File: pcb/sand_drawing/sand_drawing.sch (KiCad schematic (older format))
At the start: 13 parts, among them J0 12VDC, J1 Stepper1, J2 Stepper2, J3 Arm 1 Opto, J4 Arm 2 Opto, J5 ESP POWER, J6 Unused Pins, U1 WeMos_D1_mini, U2 LD1117_TO220

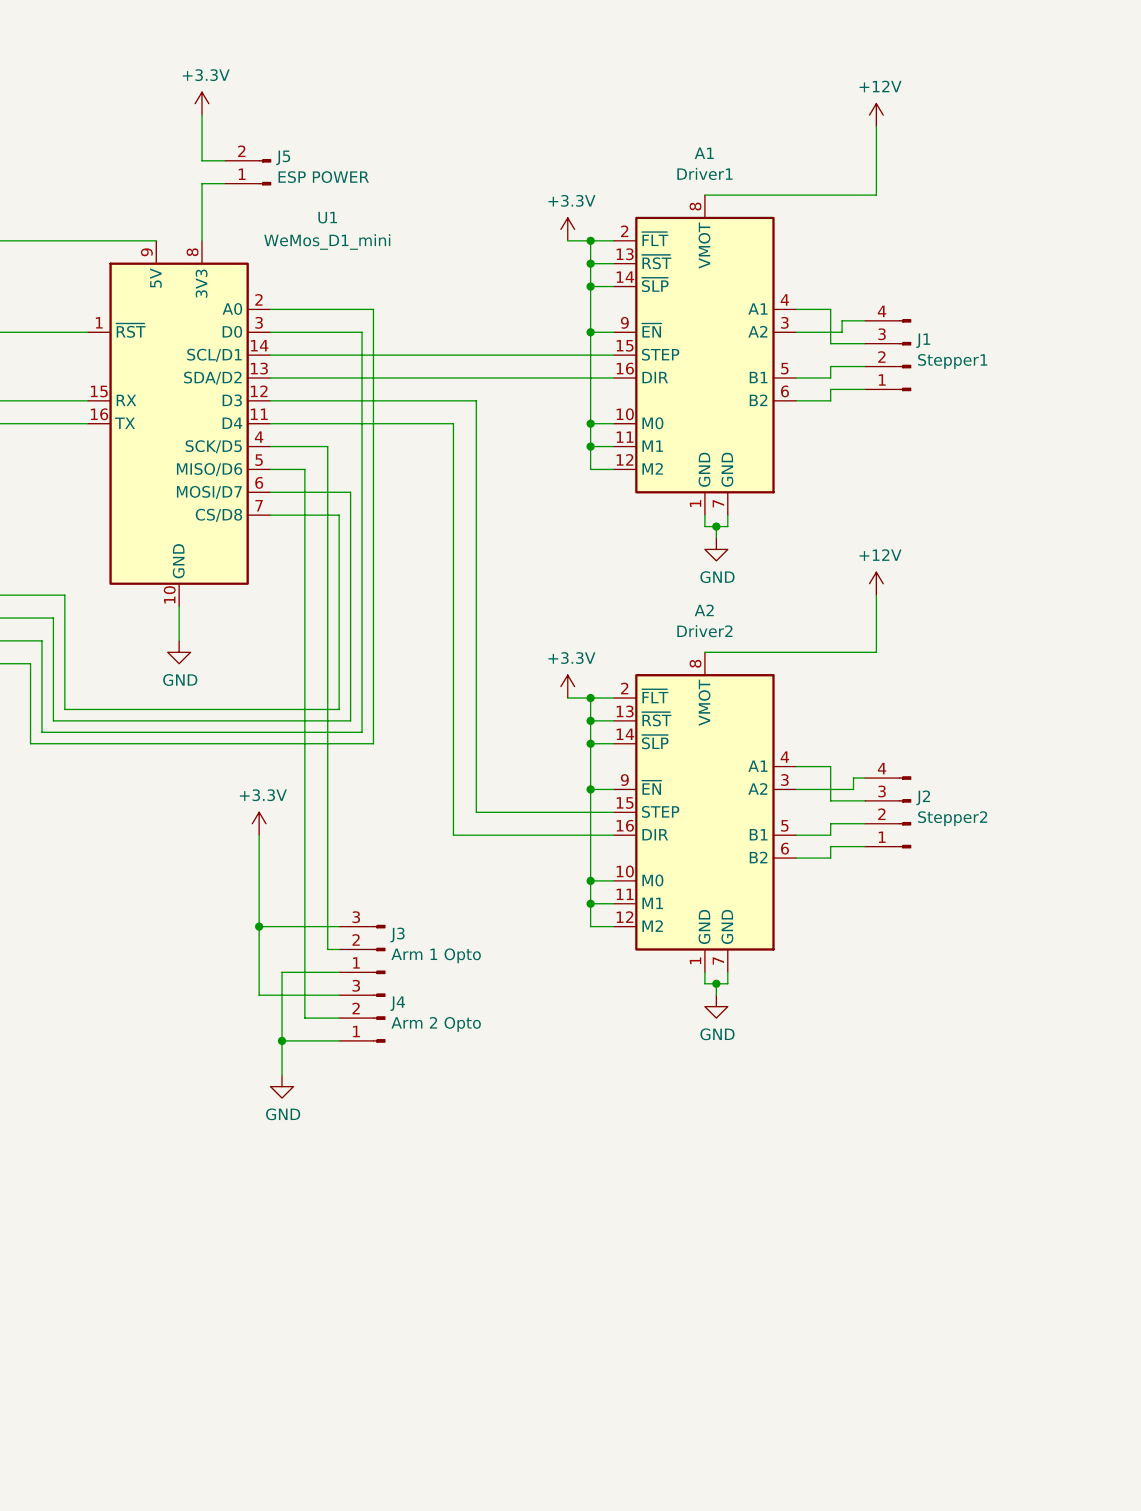
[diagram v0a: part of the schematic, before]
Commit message: Add jumpers for microstepping.
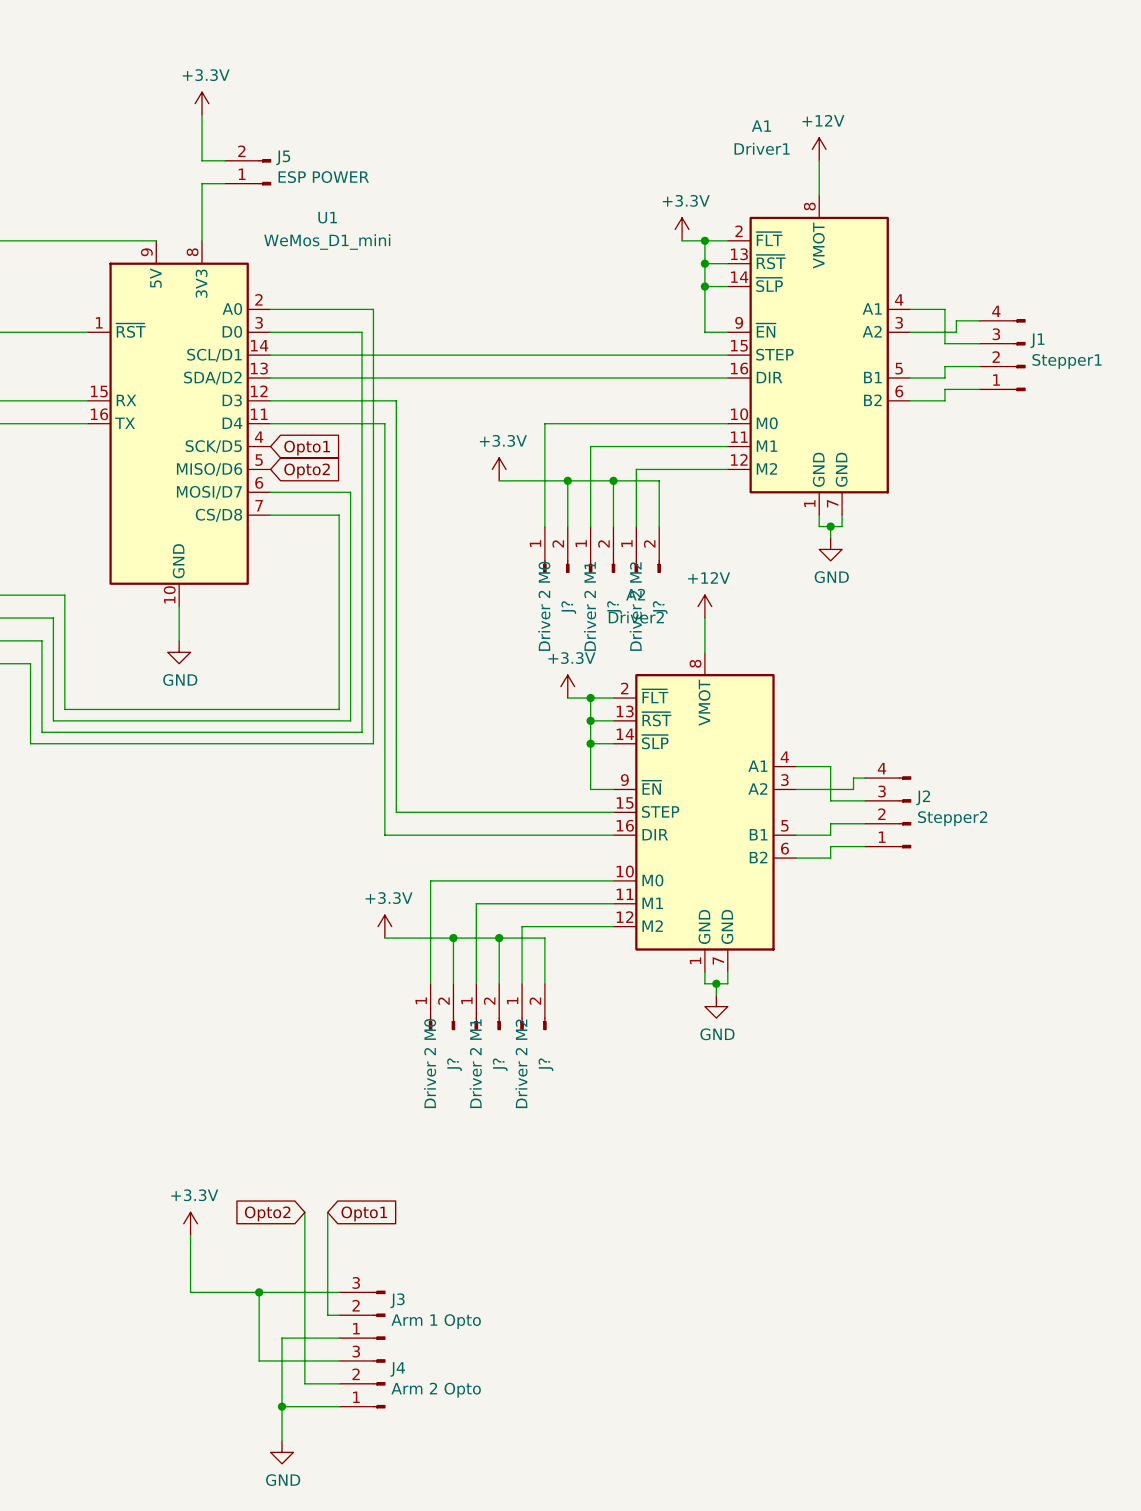
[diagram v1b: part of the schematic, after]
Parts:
- added J? (x2): Driver 2 M0, Socket_Strips:Socket_Strip_Straight_1x02_Pitch2.54mm, symbol Connector:Conn_01x02_Male
- added J? (x2): Driver 2 M1, Socket_Strips:Socket_Strip_Straight_1x02_Pitch2.54mm, symbol Connector:Conn_01x02_Male
- added J? (x2): Driver 2 M2, Socket_Strips:Socket_Strip_Straight_1x02_Pitch2.54mm, symbol Connector:Conn_01x02_Male
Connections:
- net +3V3: now also J?.2 (Pin_2), J?.2 (Pin_2), J?.2 (Pin_2), J?.2 (Pin_2), J?.2 (Pin_2), J?.2 (Pin_2); no longer A1.10 (M0), A1.11 (M1), A1.12 (M2), A2.10 (M0), A2.11 (M1), A2.12 (M2)
- net Opto1: now reaches J3.2 (Pin_2), U1.4 (SCK/D5)
- net Opto2: now reaches J4.2 (Pin_2), U1.5 (MISO/D6)
- new net: A1.10 (M0), J?.1 (Pin_1)
- new net: A1.11 (M1), J?.1 (Pin_1)
- new net: A1.12 (M2), J?.1 (Pin_1)
- new net: A2.10 (M0), J?.1 (Pin_1)
- new net: A2.11 (M1), J?.1 (Pin_1)
- new net: A2.12 (M2), J?.1 (Pin_1)
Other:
- moved on the sheet: A1, J1, J3, J4

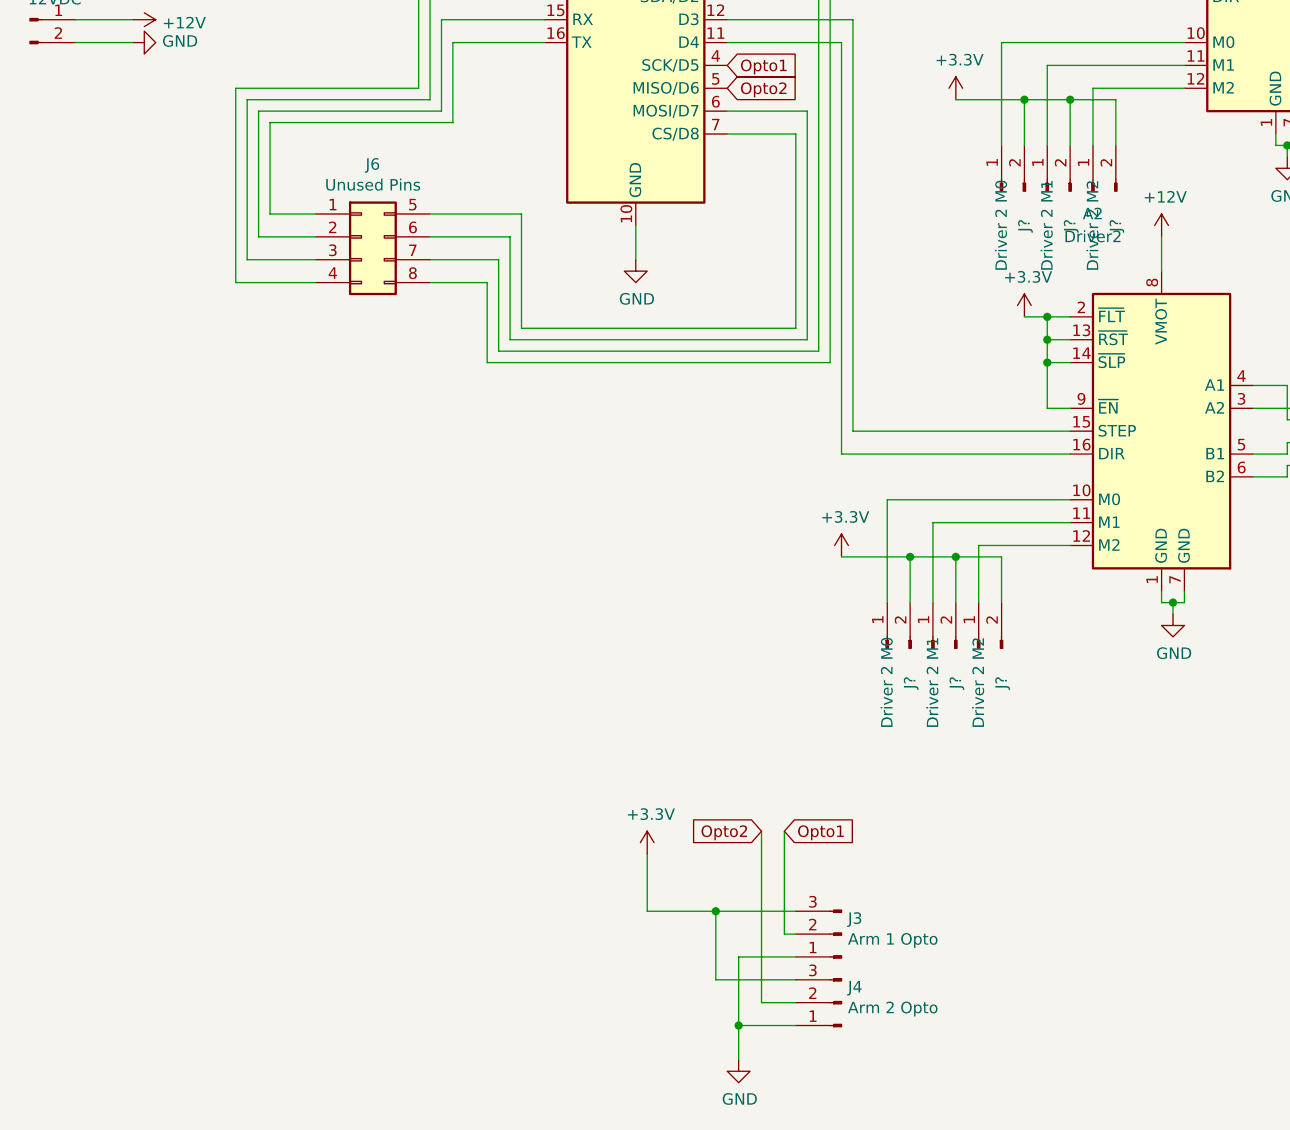
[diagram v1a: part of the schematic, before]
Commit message: Rearrange stuff, start routing.
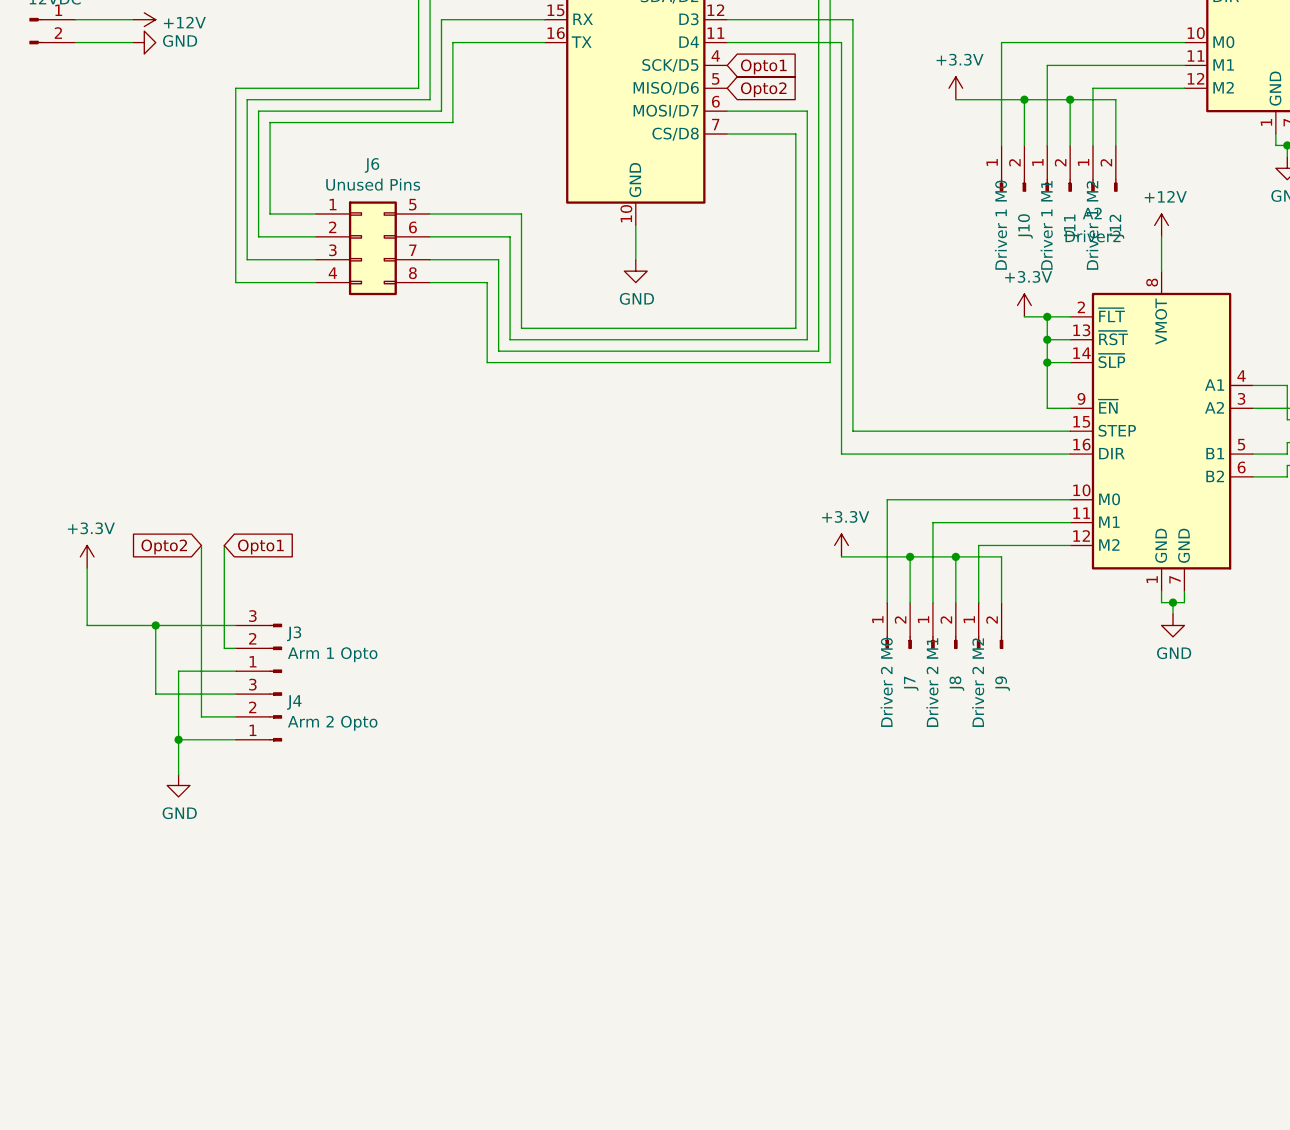
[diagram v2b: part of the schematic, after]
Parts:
- J10: renamed from J?; value Driver 2 M0 -> Driver 1 M0
- J11: renamed from J?; value Driver 2 M1 -> Driver 1 M1
- J12: renamed from J?; value Driver 2 M2 -> Driver 1 M2
- gave numbers to parts that had none: 3
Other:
- moved on the sheet: J3, J4
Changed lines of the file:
@@
 L Connector:Conn_01x03_Male J3
 U 1 1 5E9E0F06
-P 4200 6500
-F 0 "J3" H 4172 6432 50  0000 R CNN
-F 1 "Arm 1 Opto" H 4172 6523 50  0000 R CNN
-F 2 "Socket_Strips:Socket_Strip_Straight_1x03_Pitch2.54mm" H 4200 6500 50  0001 C CNN
-F 3 "~" H 4200 6500 50  0001 C CNN
-	1    4200 6500
+P 1750 5250
+F 0 "J3" H 1722 5182 50  0000 R CNN
+F 1 "Arm 1 Opto" H 1722 5273 50  0000 R CNN
+F 2 "Socket_Strips:Socket_Strip_Straight_1x03_Pitch2.54mm" H 1750 5250 50  0001 C CNN
+F 3 "~" H 1750 5250 50  0001 C CNN
+	1    1750 5250
 	-1   0    0    1
 $EndComp
@@
 L Connector:Conn_01x03_Male J4
 U 1 1 5E9E28A1
-P 4200 6800
-F 0 "J4" H 4172 6732 50  0000 R CNN
-F 1 "Arm 2 Opto" H 4172 6823 50  0000 R CNN
-F 2 "Socket_Strips:Socket_Strip_Straight_1x03_Pitch2.54mm" H 4200 6800 50  0001 C CNN
-F 3 "~" H 4200 6800 50  0001 C CNN
-	1    4200 6800
+P 1750 5550
+F 0 "J4" H 1722 5482 50  0000 R CNN
+F 1 "Arm 2 Opto" H 1722 5573 50  0000 R CNN
+F 2 "Socket_Strips:Socket_Strip_Straight_1x03_Pitch2.54mm" H 1750 5550 50  0001 C CNN
+F 3 "~" H 1750 5550 50  0001 C CNN
+	1    1750 5550
 	-1   0    0    1
 $EndComp
@@
 L power:GND #PWR0105
 U 1 1 5E9E4C25
-P 3750 7050
-F 0 "#PWR0105" H 3750 6800 50  0001 C CNN
-F 1 "GND" H 3755 6877 50  0000 C CNN
-F 2 "" H 3750 7050 50  0001 C CNN
-F 3 "" H 3750 7050 50  0001 C CNN
-	1    3750 7050
-	1    0    0    -1
-$EndComp
-Wire Wire Line
-	3750 7050 3750 6900
-Connection ~ 3750 6900
-Wire Wire Line
-	3750 6900 3750 6600
-Wire Wire Line
-	4000 6500 3950 6500
+P 1300 5800
+F 0 "#PWR0105" H 1300 5550 50  0001 C CNN
+F 1 "GND" H 1305 5627 50  0000 C CNN
+F 2 "" H 1300 5800 50  0001 C CNN
+F 3 "" H 1300 5800 50  0001 C CNN
+	1    1300 5800
+	1    0    0    -1
+$EndComp
+Wire Wire Line
+	1300 5800 1300 5650
+Connection ~ 1300 5650
+Wire Wire Line
+	1300 5650 1300 5350
+Wire Wire Line
+	1550 5250 1500 5250
 $Comp
 L power:+3.3V #PWR0106
@@
 L power:+3.3V #PWR0109
 U 1 1 5E9FE0CA
-P 3350 6150
-F 0 "#PWR0109" H 3350 6000 50  0001 C CNN
-F 1 "+3.3V" H 3365 6323 50  0000 C CNN
-F 2 "" H 3350 6150 50  0001 C CNN
-F 3 "" H 3350 6150 50  0001 C CNN
-	1    3350 6150
-	1    0    0    -1
-$EndComp
-Wire Wire Line
-	3850 6800 4000 6800
-Wire Wire Line
-	3650 6700 4000 6700
-Wire Wire Line
-	4000 6400 3650 6400
-Connection ~ 3650 6400
-Wire Wire Line
-	3650 6400 3650 6700
-Wire Wire Line
-	3750 6600 4000 6600
-Wire Wire Line
-	3750 6900 4000 6900
+P 900 4900
+F 0 "#PWR0109" H 900 4750 50  0001 C CNN
+F 1 "+3.3V" H 915 5073 50  0000 C CNN
+F 2 "" H 900 4900 50  0001 C CNN
+F 3 "" H 900 4900 50  0001 C CNN
+	1    900  4900
+	1    0    0    -1
+$EndComp
+Wire Wire Line
+	1400 5550 1550 5550
+Wire Wire Line
+	1200 5450 1550 5450
+Wire Wire Line
+	1550 5150 1200 5150
+Connection ~ 1200 5150
+Wire Wire Line
+	1200 5150 1200 5450
+Wire Wire Line
+	1300 5350 1550 5350
+Wire Wire Line
+	1300 5650 1550 5650
 Wire Wire Line
 	3700 2500 4250 2500
@@
 	2650 3650 2400 3650
 $Comp
-L Connector:Conn_01x02_Male J?
+L Connector:Conn_01x02_Male J7
 U 1 1 5E99CB34
 P 4400 5250
-F 0 "J?" H 4250 5150 50  0000 C CNN
+F 0 "J7" H 4250 5150 50  0000 C CNN
 F 1 "Driver 2 M0" H 4250 5250 50  0000 C CNN
 F 2 "Socket_Strips:Socket_Strip_Straight_1x02_Pitch2.54mm" H 4400 5250 50  0001 C CNN
@@
 $EndComp
 $Comp
-L Connector:Conn_01x02_Male J?
+L Connector:Conn_01x02_Male J8
 U 1 1 5E9C5CF2
 P 4600 5250
-F 0 "J?" H 4450 5150 50  0000 C CNN
+F 0 "J8" H 4450 5150 50  0000 C CNN
 F 1 "Driver 2 M1" H 4450 5250 50  0000 C CNN
 F 2 "Socket_Strips:Socket_Strip_Straight_1x02_Pitch2.54mm" H 4600 5250 50  0001 C CNN
@@
 $EndComp
 $Comp
-L Connector:Conn_01x02_Male J?
+L Connector:Conn_01x02_Male J9
 U 1 1 5E9C5F13
 P 4800 5250
-F 0 "J?" H 4650 5150 50  0000 C CNN
+F 0 "J9" H 4650 5150 50  0000 C CNN
 F 1 "Driver 2 M2" H 4650 5250 50  0000 C CNN
 F 2 "Socket_Strips:Socket_Strip_Straight_1x02_Pitch2.54mm" H 4800 5250 50  0001 C CNN
@@
 Text GLabel 3700 2800 2    50   Input ~ 0
 Opto2
-Text GLabel 3850 6050 0    50   Input ~ 0
+Text GLabel 1400 4800 0    50   Input ~ 0
 Opto2
-Text GLabel 3950 6050 2    50   Input ~ 0
+Text GLabel 1500 4800 2    50   Input ~ 0
 Opto1
 Wire Wire Line
-	3950 6050 3950 6500
-Wire Wire Line
-	3650 6400 3350 6400
-Wire Wire Line
-	3350 6400 3350 6150
-Wire Wire Line
-	3850 6800 3850 6050
+	1500 4800 1500 5250
+Wire Wire Line
+	1200 5150 900  5150
+Wire Wire Line
+	900  5150 900  4900
+Wire Wire Line
+	1400 5550 1400 4800
 Wire Wire Line
 	4200 2600 4200 4400
@@
 	4800 4800 4800 5050
 $Comp
-L power:+3.3V #PWR?
+L power:+3.3V #PWR0116
 U 1 1 5EA0D498
 P 4200 4850
-F 0 "#PWR?" H 4200 4700 50  0001 C CNN
+F 0 "#PWR0116" H 4200 4700 50  0001 C CNN
 F 1 "+3.3V" H 4215 5023 50  0000 C CNN
 F 2 "" H 4200 4850 50  0001 C CNN
@@
 	5600 3600 5600 3450
 $Comp
-L Connector:Conn_01x02_Male J?
+L Connector:Conn_01x02_Male J10
 U 1 1 5EA4E3CF
 P 4900 3250
-F 0 "J?" H 4750 3150 50  0000 C CNN
-F 1 "Driver 2 M0" H 4750 3250 50  0000 C CNN
+F 0 "J10" H 4750 3150 50  0000 C CNN
+F 1 "Driver 1 M0" H 4750 3250 50  0000 C CNN
 F 2 "Socket_Strips:Socket_Strip_Straight_1x02_Pitch2.54mm" H 4900 3250 50  0001 C CNN
 F 3 "~" H 4900 3250 50  0001 C CNN
@@
 $EndComp
 $Comp
-L Connector:Conn_01x02_Male J?
+L Connector:Conn_01x02_Male J11
 U 1 1 5EA4E3D5
 P 5100 3250
-F 0 "J?" H 4950 3150 50  0000 C CNN
-F 1 "Driver 2 M1" H 4950 3250 50  0000 C CNN
+F 0 "J11" H 4950 3150 50  0000 C CNN
+F 1 "Driver 1 M1" H 4950 3250 50  0000 C CNN
 F 2 "Socket_Strips:Socket_Strip_Straight_1x02_Pitch2.54mm" H 5100 3250 50  0001 C CNN
 F 3 "~" H 5100 3250 50  0001 C CNN
@@
 $EndComp
 $Comp
-L Connector:Conn_01x02_Male J?
+L Connector:Conn_01x02_Male J12
 U 1 1 5EA4E3DB
 P 5300 3250
-F 0 "J?" H 5150 3150 50  0000 C CNN
-F 1 "Driver 2 M2" H 5150 3250 50  0000 C CNN
+F 0 "J12" H 5150 3150 50  0000 C CNN
+F 1 "Driver 1 M2" H 5150 3250 50  0000 C CNN
 F 2 "Socket_Strips:Socket_Strip_Straight_1x02_Pitch2.54mm" H 5300 3250 50  0001 C CNN
 F 3 "~" H 5300 3250 50  0001 C CNN
@@
 	5300 2800 5300 3050
 $Comp
-L power:+3.3V #PWR?
+L power:+3.3V #PWR0117
 U 1 1 5EA4E3E7
 P 4700 2850
-F 0 "#PWR?" H 4700 2700 50  0001 C CNN
+F 0 "#PWR0117" H 4700 2700 50  0001 C CNN
 F 1 "+3.3V" H 4715 3023 50  0000 C CNN
 F 2 "" H 4700 2850 50  0001 C CNN
